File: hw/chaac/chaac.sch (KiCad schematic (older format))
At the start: 74 parts, among them J1 windrain, J10 Solar Panel, J11 FAN, J12 GPS, J2 Conn_01x02, J3 UART, J4 Battery, J5 Power, J6 Light, J7 AM2315, J8 TC2030-CTX, J9 Therm, SW1 RST, U1 MIC550X, U2 STM32L432, U3 XBEE_S2C, U5 BMP280, U6 MCP73871, U7 XCL102, Y1 32.768kHz

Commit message: Updated Chaac HW to v1.1
Added gate for controlling power to wind direction sensor and light sensor.
(This should allow for power gating for lower power consumption)

Removed all GPS stuff (won't be using it this time)

Removed fan driver. (also won't be using it)

Added pull down resistors on xbee enable and boot0.

Fixed battery charger bug (PROG1 and PROG2 were flipped)
Added 1k resistor to therm pin

Flipped wind/rain connector location for simpler routing
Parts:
- removed C29, C30: 10uF, Capacitor_SMD:C_0805_2012Metric, symbol Device:C_Small
- removed J11: FAN, Connector_PinHeader_2.54mm:PinHeader_1x02_P2.54mm_Vertical, symbol Connector_Generic:Conn_01x02
- removed J12: GPS, Connector_PinHeader_2.54mm:PinHeader_1x04_P2.54mm_Vertical, symbol Connector_Generic:Conn_01x04
- removed U7: XCL102, alvarop:XCL102, symbol alvarop:XCL102
- added C6: 0.01 uF, Capacitor_SMD:C_0603_1608Metric, symbol Device:C_Small
- added C7: DNP, Capacitor_SMD:C_0603_1608Metric, symbol Device:C_Small
- added Q1: Q_PMOS_GSD, Package_TO_SOT_SMD:SOT-23, symbol Device:Q_PMOS_GSD
- added R14, R27: 10k, Resistor_SMD:R_0603_1608Metric, symbol Device:R_Small
- added R26: 1k, Resistor_SMD:R_0603_1608Metric, symbol Device:R_Small
- C10, C14: value 0.01 uF -> 0.1uF; DKPN 311-1085-1-ND -> 490-1532-1-ND; MPN CC0603KRX7R9BB103 -> GRM188R71C104KA01D
- R11: value 0 -> 10k; DKPN 311-0.0GRCT-ND -> 311-10.0KHRCT-ND; MPN RC0603JR-070RL -> RC0603FR-0710KL
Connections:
- net labels added: SNS_3V3, SNS_3V3_EN
- net labels removed: FAN, FAN_EN, GPS_SBY, GPS_TX, STAT1, STAT2, WDIR_EN, nPG
- wire segments 346 -> 332
- no-connect marks 20 -> 24
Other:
- moved on the sheet: R1, R15, R18, R2, R3, R4, R5, R6

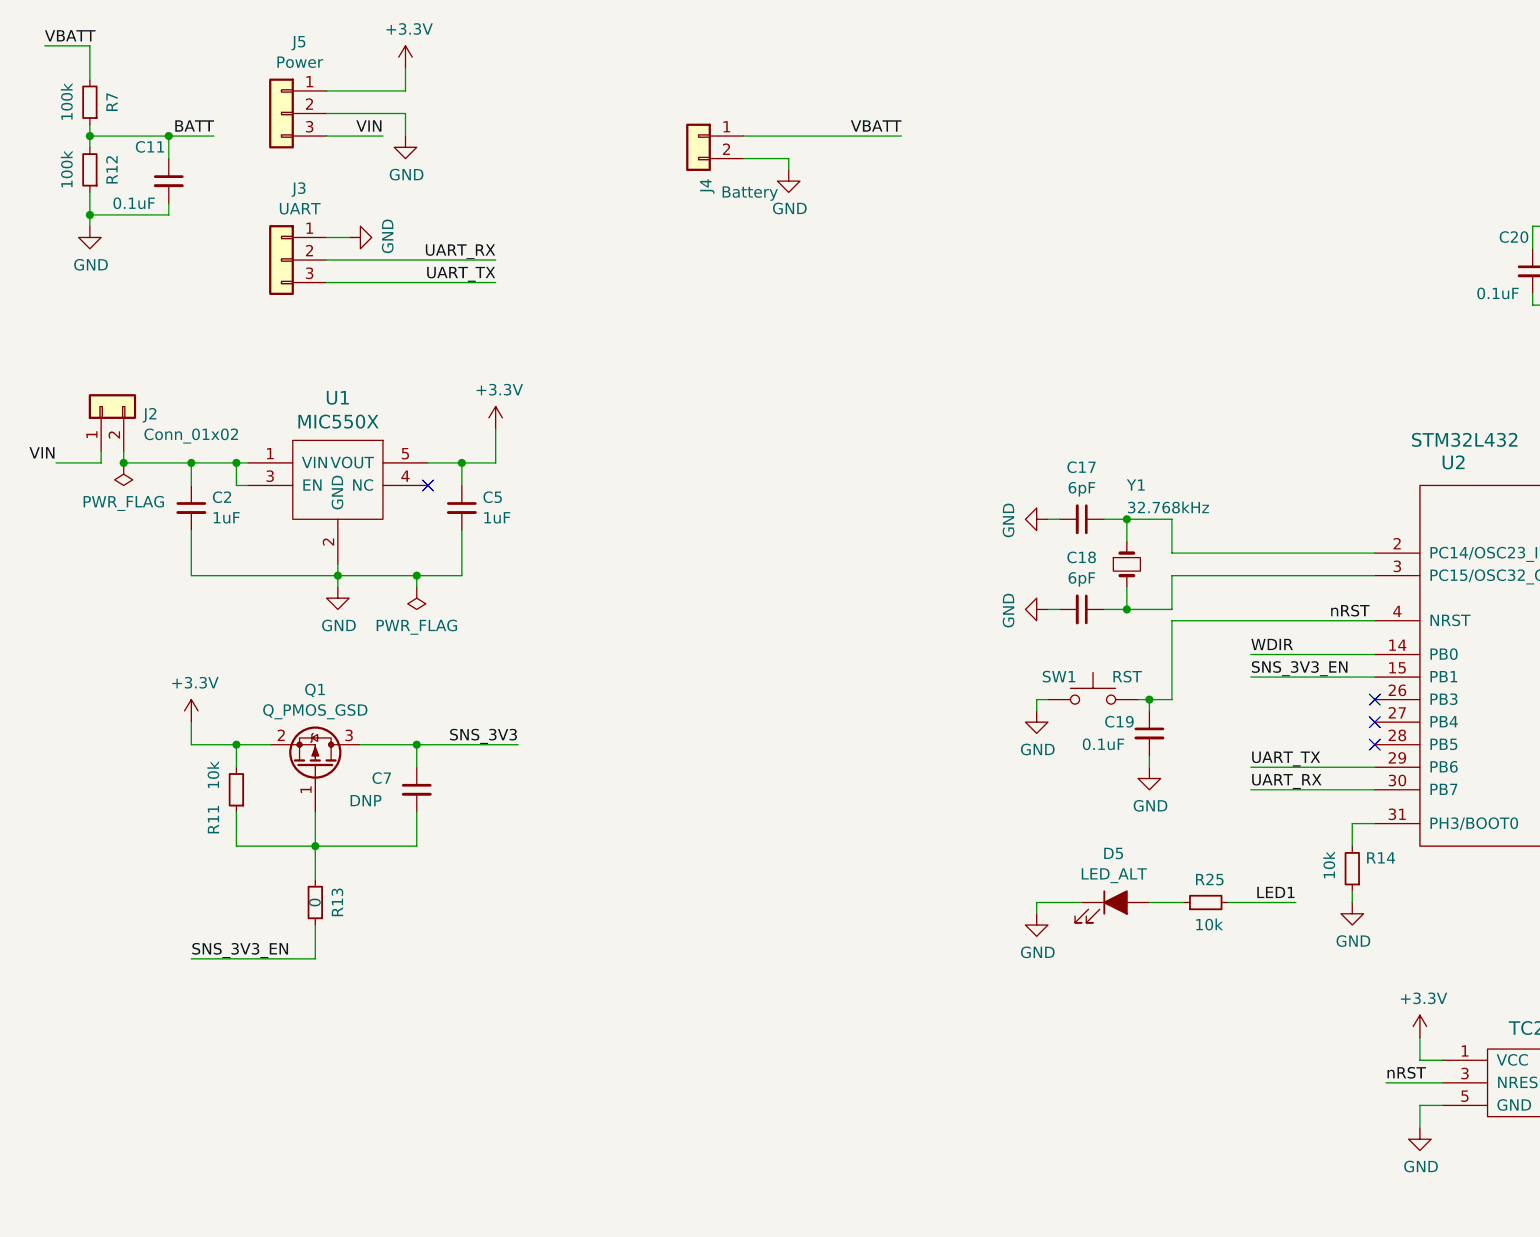
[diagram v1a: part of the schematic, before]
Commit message: Did layout/schematic for chaac v1.2
Added extra led, boot button, and sense resistors for solar panel voltage
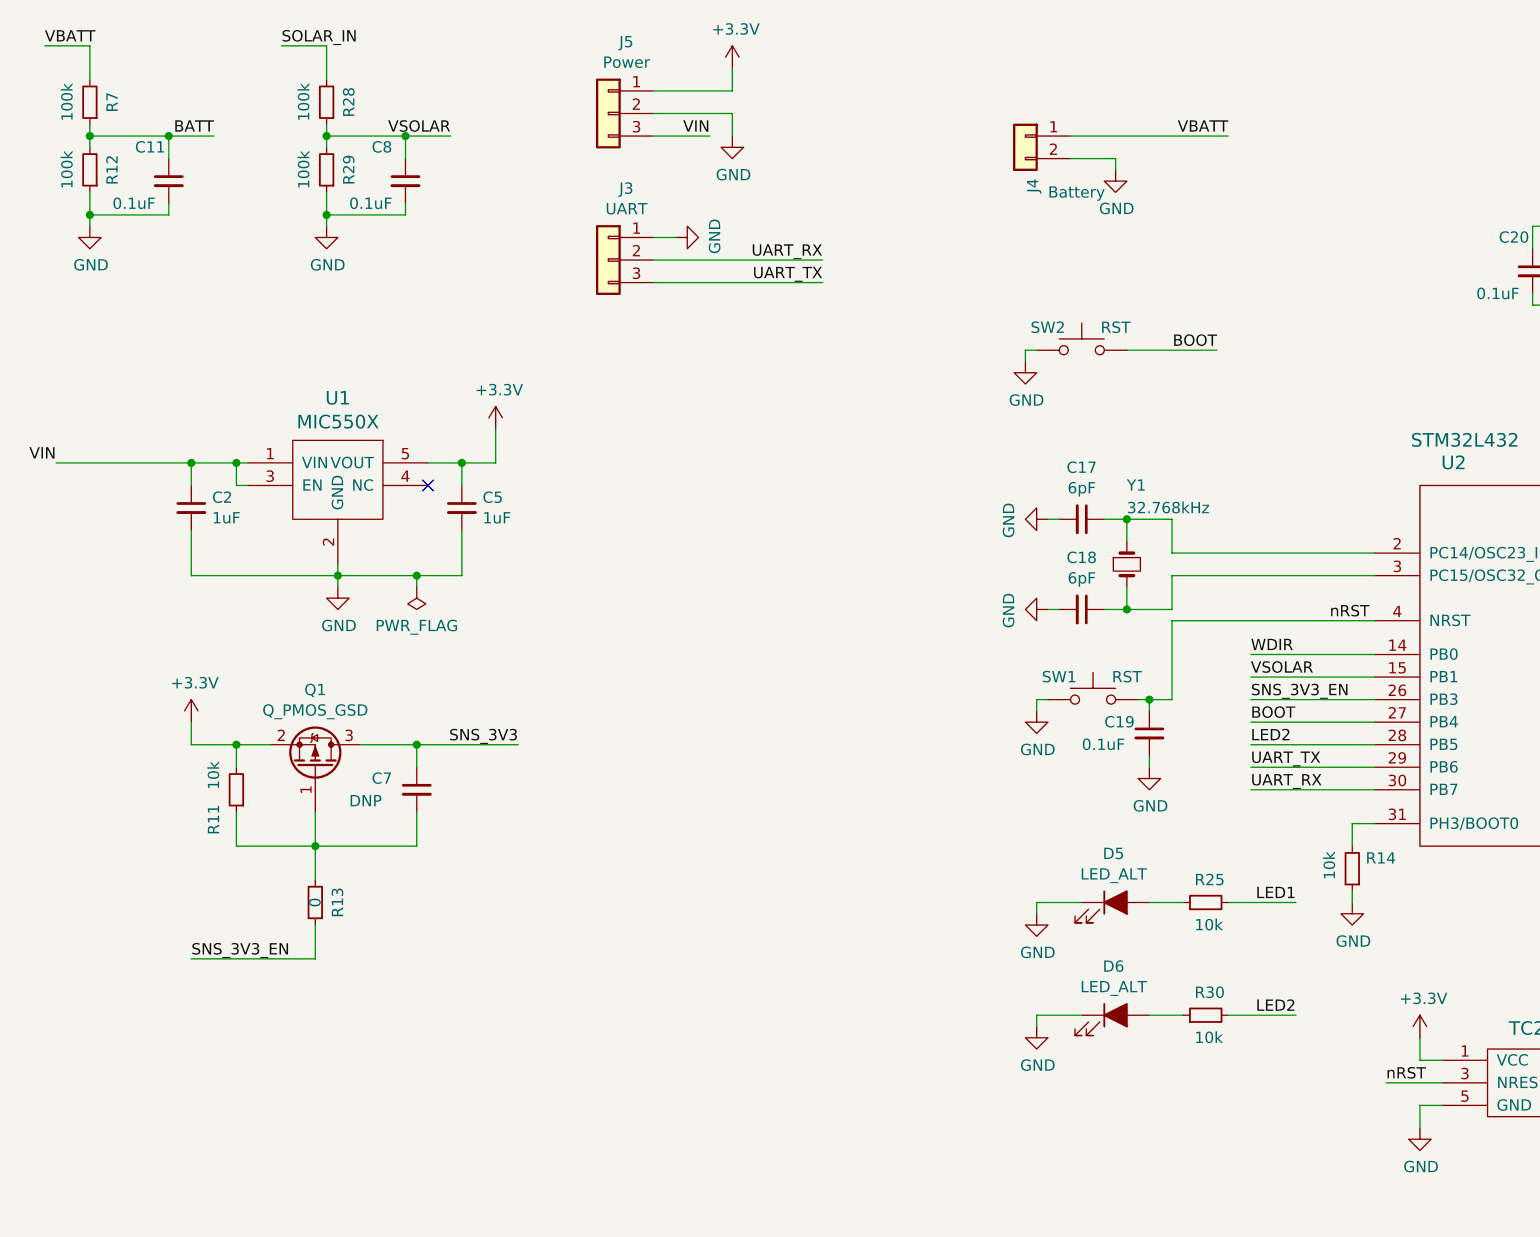
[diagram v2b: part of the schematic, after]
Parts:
- removed J2: Conn_01x02, Connector_PinHeader_2.54mm:PinHeader_1x02_P2.54mm_Vertical, symbol Connector_Generic:Conn_01x02
- added C8: 0.1uF, Capacitor_SMD:C_0603_1608Metric, symbol Device:C_Small
- added D6: LED_ALT, LED_SMD:LED_0603_1608Metric, symbol Device:LED_ALT
- added R28, R29: 100k, Resistor_SMD:R_0603_1608Metric, symbol Device:R_Small
- added R30: 10k, Resistor_SMD:R_0603_1608Metric, symbol Device:R_Small
- added SW2: RST, alvarop:PTS645SM43SMTR92, symbol Switch:SW_Push
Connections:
- net GND: now also C8.2, D6.1 (K), R29.1, SW2.1
- net SNS_3V3_EN: now also U2.26 (PB3); no longer U2.15 (PB1)
- net SOLAR_IN: now also R28.2
- net VIN: now also C2.1, U1.1 (VIN), U1.3 (EN)
- net BOOT: now reaches U2.27 (PB4)
- net BOOT: now also SW2.2
- net LED2: now reaches U2.28 (PB5)
- net LED2: now also R30.2
- new net: D6.2 (A), R30.1
- new net VSOLAR: C8.1, R28.1, R29.2, U2.15 (PB1)
- no-connect marks 24 -> 21
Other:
- moved on the sheet: J3, J4, J5

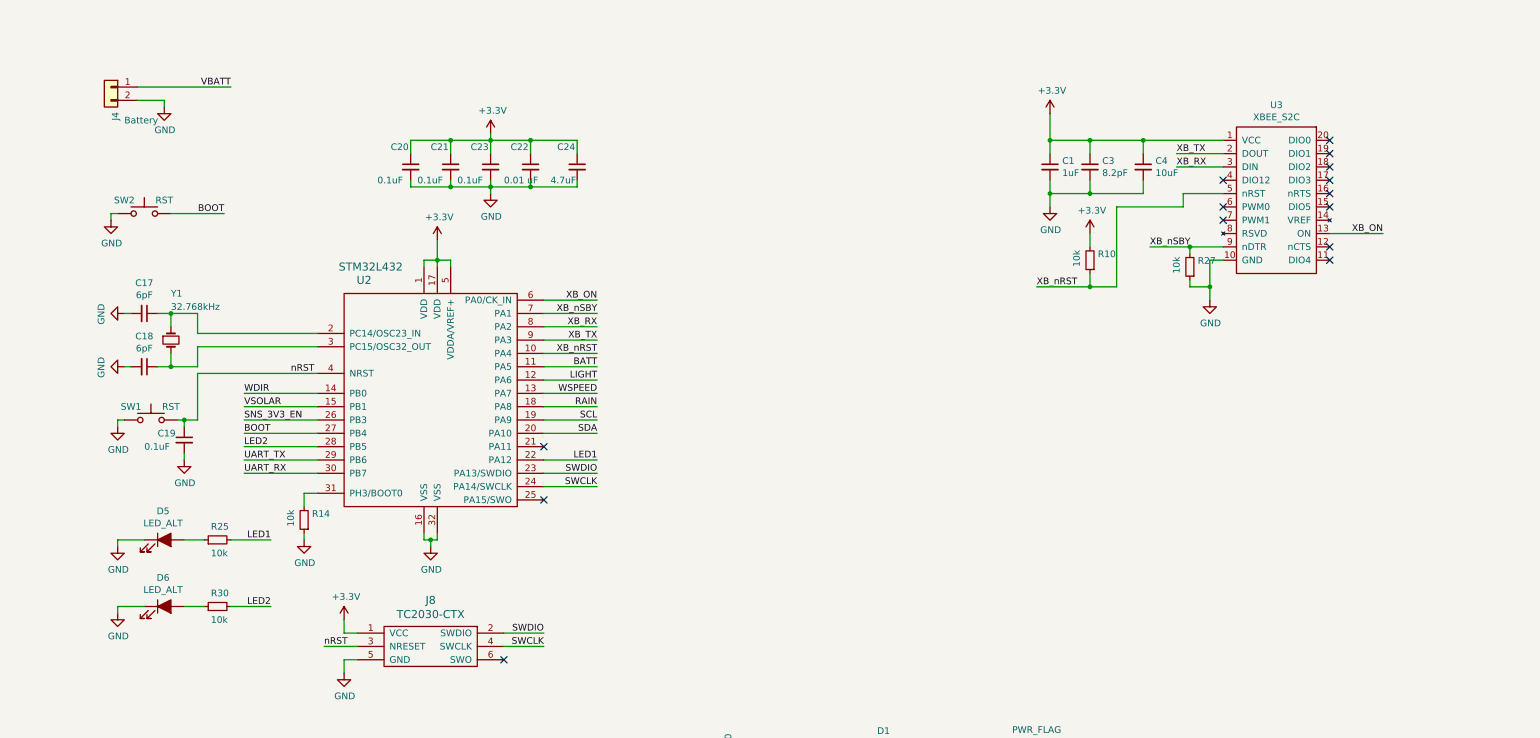
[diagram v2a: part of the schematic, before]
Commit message: Swapping processor for NRF52811
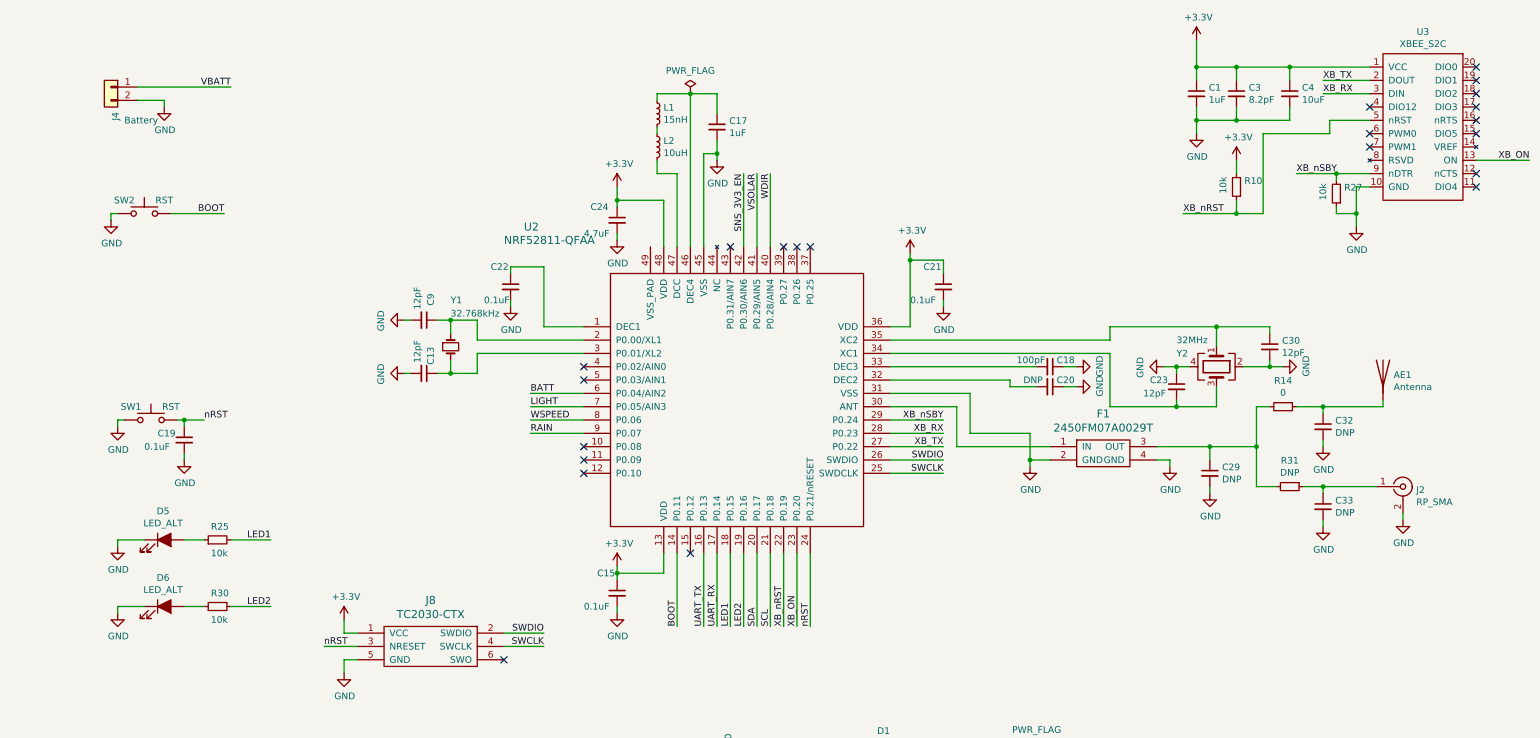
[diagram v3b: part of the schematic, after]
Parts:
- removed U2: STM32L432, alvarop:UFQFPN32, symbol alvarop:STM32L432
- added AE1: Antenna, alvarop:AMCA31-2R450G-S1F-T3, symbol Device:Antenna
- added C13, C30, C9: 12pF, Capacitor_SMD:C_0402_1005Metric, symbol Device:C_Small
- added C15: 0.1uF, Capacitor_SMD:C_0402_1005Metric, symbol Device:C_Small
- added C29, C32, C33: DNP, Capacitor_SMD:C_0402_1005Metric, symbol Device:C_Small
- added F1: 2450FM07A0029T, alvarop:2450FM07A0029T, symbol alvarop:2450FM07A0029T
- added J2: RP_SMA, Connector_Coaxial:SMA_Samtec_SMA-J-P-H-ST-EM1_EdgeMount, symbol Connector:Conn_Coaxial
- added L1: 15nH, Inductor_SMD:L_0402_1005Metric, symbol Device:L_Small
- added L2: 10uH, Inductor_SMD:L_0603_1608Metric, symbol Device:L_Small
- added R31: DNP, Resistor_SMD:R_0402_1005Metric, symbol Device:R_Small
- added U2: NRF52811-QFAA, alvarop:LQFP48, symbol alvarop:NRF52811-QFAA
- added Y2: 32MHz, Crystal:Crystal_SMD_2016-4Pin_2.0x1.6mm, symbol Device:Crystal_GND24
- C17: value 6pF -> 1uF; footprint Capacitor_SMD:C_0603_1608Metric -> Capacitor_SMD:C_0402_1005Metric; DKPN 1276-2134-1-ND -> (none); MPN CL10C060DB8NNNC -> (none)
- C18: value 6pF -> 100pF; footprint Capacitor_SMD:C_0603_1608Metric -> Capacitor_SMD:C_0402_1005Metric; DKPN 1276-2134-1-ND -> (none); MPN CL10C060DB8NNNC -> (none)
- C20: value 0.1uF -> DNP
- C21: footprint Capacitor_SMD:C_0603_1608Metric -> Capacitor_SMD:C_0402_1005Metric; DKPN 490-1532-1-ND -> (none); MPN GRM188R71C104KA01D -> (none)
- C22: value 0.01 uF -> 0.1uF; footprint Capacitor_SMD:C_0603_1608Metric -> Capacitor_SMD:C_0402_1005Metric; DKPN 311-1085-1-ND -> (none); MPN CC0603KRX7R9BB103 -> (none)
- C23: value 0.1uF -> 12pF; footprint Capacitor_SMD:C_0603_1608Metric -> Capacitor_SMD:C_0402_1005Metric; DKPN 490-1532-1-ND -> (none); MPN GRM188R71C104KA01D -> (none)
- R14: value 10k -> 0; footprint Resistor_SMD:R_0603_1608Metric -> Resistor_SMD:R_0402_1005Metric; DKPN 311-10.0KHRCT-ND -> (none); MPN RC0603FR-0710KL -> (none)
- Y1: DKPN 644-1171-1-ND -> (none); MPN NX3215SA-32.768K-STD-MUA-14 -> (none)
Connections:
- net +3V3: now also C15.1, U2.13 (VDD), U2.36 (VDD), U2.48 (VDD); no longer C20.1, C22.1, C23.1
- net BATT: now also U2.6 (P0.04/AIN2)
- net BOOT: now also U2.14 (P0.11)
- net GND: now also C18.1, C20.1, C23.1, C13.2, C15.2, C29.2, C30.2, C32.2, C33.2, C9.2, F1.2 (GND), F1.4 (GND), J2.2 (Ext), U2.31 (VSS), U2.45 (VSS), Y2.2, Y2.4; no longer C18.2, C20.2, C23.2, R14.1
- net LED1: now also U2.18 (P0.15)
- net LED2: now also U2.19 (P0.16)
- net LIGHT: now also U2.7 (P0.05/AIN3)
- net RAIN: now also U2.9 (P0.07)
- net SCL: now also U2.21 (P0.18)
- net SDA: now also U2.20 (P0.17)
- net SNS_3V3_EN: now also U2.42 (P0.30/AIN6)
- net SWCLK: now also U2.25 (SWDCLK)
- net SWDIO: now also U2.26 (SWDIO)
- net UART_RX: now also U2.17 (P0.14)
- net UART_TX: now also U2.16 (P0.13)
- net VSOLAR: now also U2.41 (P0.29/AIN5)
- net WDIR: now also U2.40 (P0.28/AIN4)
- net WSPEED: now also U2.8 (P0.06)
- net XB_ON: now also U2.23 (P0.20)
- net XB_RX: now also U2.28 (P0.23)
- net XB_TX: now also U2.27 (P0.22)
- net XB_nRST: now also U2.22 (P0.19)
- net XB_nSBY: now also U2.29 (P0.24)
- net nRST: now also U2.24 (P0.21/nRESET)
- net at Y1.1: now also C9.1, U2.2 (P0.00/XL1); no longer C17.1
- net at Y1.2: now also C13.1, U2.3 (P0.01/XL2); no longer C18.1
- net at R14.2: now also C29.1, F1.3 (OUT), R31.2
- new net: C22.1, U2.1 (DEC1)
- new net: F1.1 (IN), U2.30 (ANT)
- new net: C20.2, U2.32 (DEC2)
- new net: C18.2, U2.33 (DEC3)
- new net: C23.2, U2.34 (XC1), Y2.3
- new net: C30.1, U2.35 (XC2), Y2.1
- new net: C17.1, L1.1, U2.46 (DEC4)
- new net: L2.2, U2.47 (DCC)
- new net: L1.2, L2.1
- new net: C33.1, J2.1 (In), R31.1
- new net: AE1.1 (A), C32.1, R14.1
- no-connect marks 21 -> 29
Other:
- moved on the sheet: C1, C21, C22, C24, C3, C4, R10, R27, U3, Y1
